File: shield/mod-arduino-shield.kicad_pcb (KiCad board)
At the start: 2 copper layers, 68.7 x 53.3 mm, 49 parts, among them J1 RJHSE-5084, J2 RJHSE-5084, Q1 MMBT3904, U1 SN75176BDR

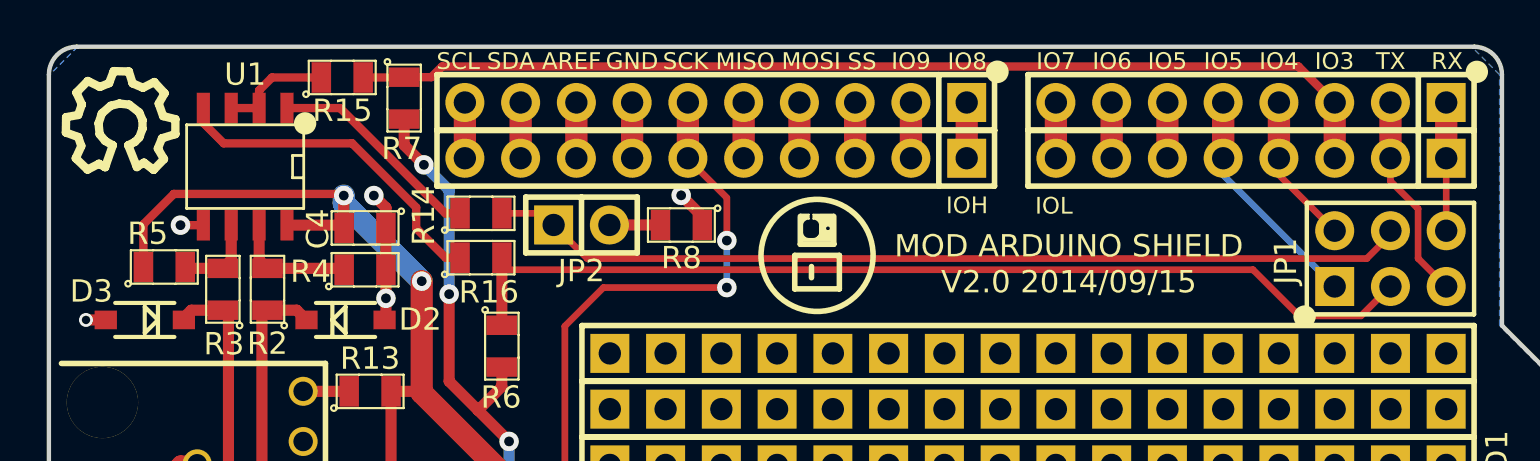
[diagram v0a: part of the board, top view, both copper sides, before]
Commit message: fix issue #3: Add "CC by-SA" license logo to the PCB silk layer Added MOD logo and improved/rearranged previous silk text.
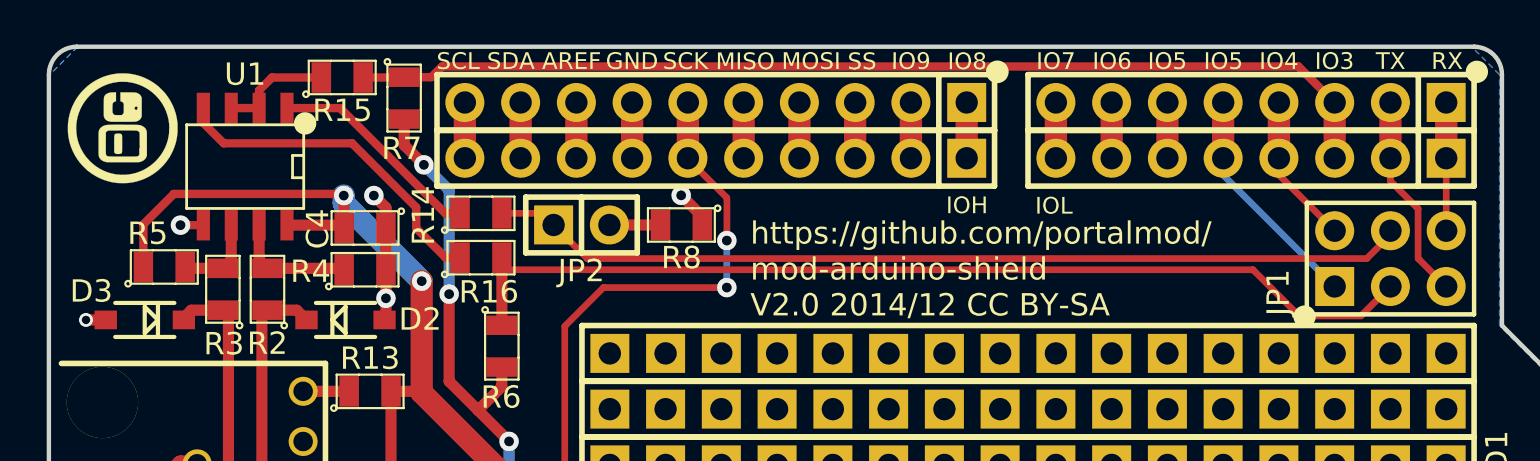
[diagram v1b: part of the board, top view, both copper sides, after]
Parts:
- removed REF***: VAL***, mod-arduino-shield-lib:Symbol_OSHW-Logo_SilkScreen
- added LOGO: LOGO, MOD_Footprints_Lib:MOD_Logo_Small, F.Cu at (99.7, 69.8)
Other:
- board text added: "https://github.com/portalmod/ mod-arduino-shield V2.0 2014/12 CC BY-SA"
- board text removed: "MOD ARDUINO SHIELD V2.0 2014/09/15"

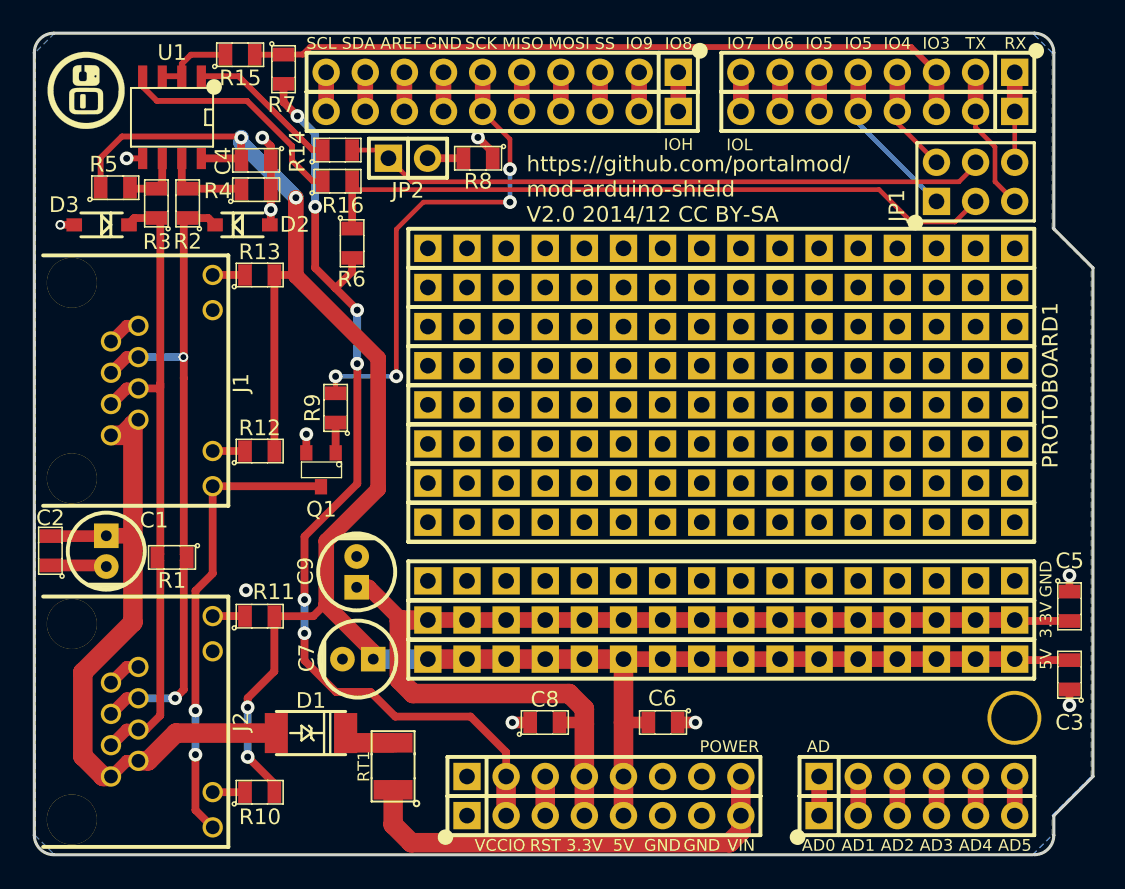
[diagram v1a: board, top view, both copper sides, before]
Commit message: fix issue #6: use same labels on shield as used in arduino
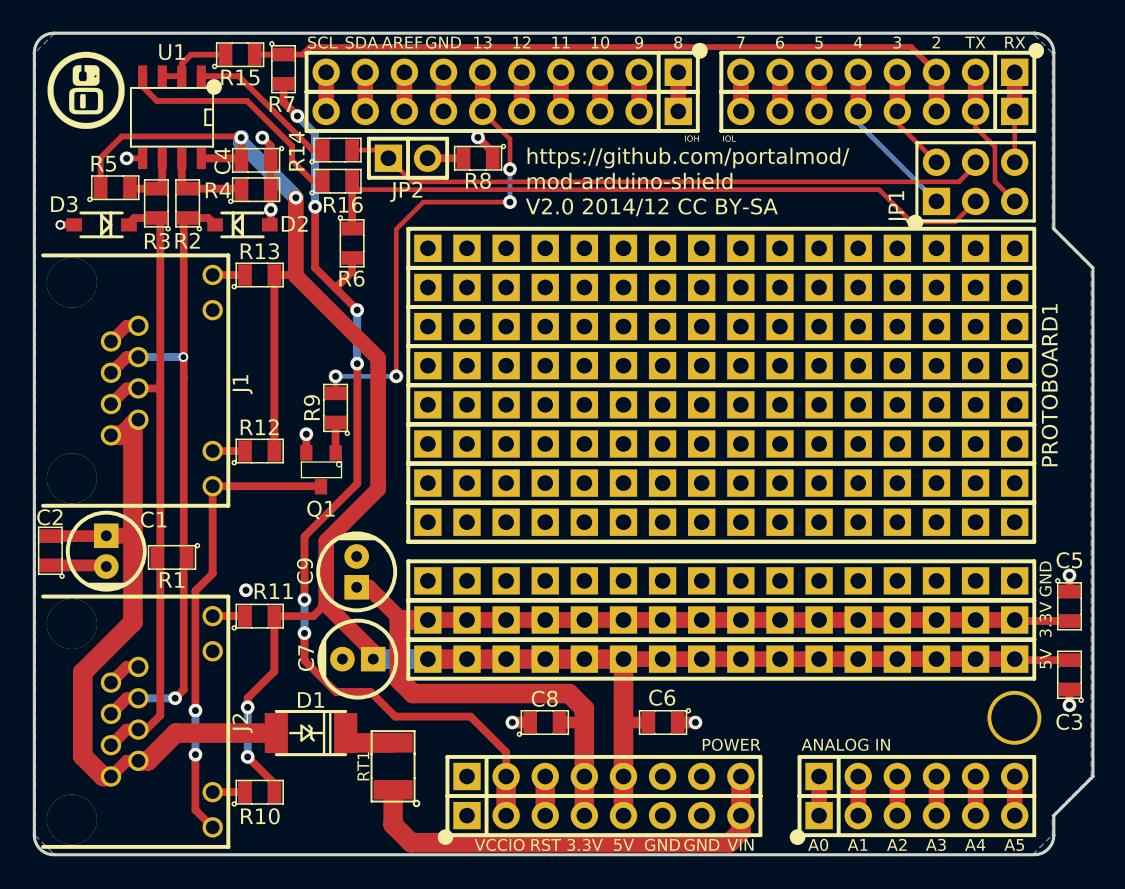
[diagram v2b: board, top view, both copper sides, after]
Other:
- board text added: "10"
- board text added: "11"
- board text added: "12"
- board text added: "13"
- board text added: "2"
- board text added: "3"
- board text added: "4"
- board text added: "5"
- board text added: "6"
- board text added: "7"
- board text added: "8"
- board text added: "9"
- board text added: "A0"
- board text added: "A1"
- board text added: "A2"
- board text added: "A3"
- board text added: "A4"
- board text added: "A5"
- board text added: "ANALOG IN"
- board text removed: "AD"
- board text removed: "AD0"
- board text removed: "AD1"
- board text removed: "AD2"
- board text removed: "AD3"
- board text removed: "AD4"
- board text removed: "AD5"
- board text removed: "IO3"
- board text removed: "IO4"
- board text removed: "IO5"
- board text removed: "IO6"
- board text removed: "IO7"
- board text removed: "IO8"
- board text removed: "IO9"
- board text removed: "MISO"
- board text removed: "MOSI"
- board text removed: "SCK"
- board text removed: "SS"

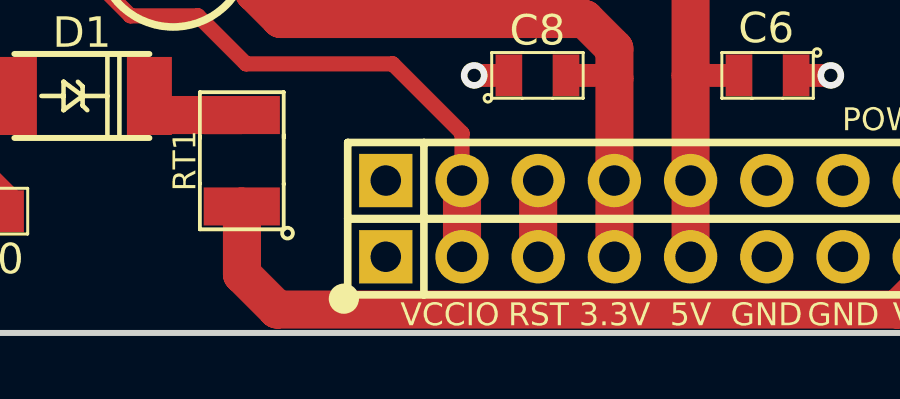
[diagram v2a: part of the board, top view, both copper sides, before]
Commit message: fix issue #2: rename VCCIO to IOREF
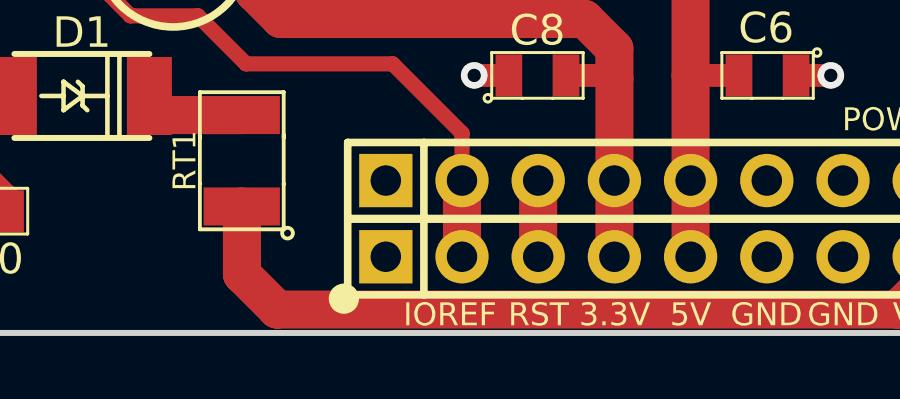
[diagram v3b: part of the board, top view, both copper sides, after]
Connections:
- net VCCIO renamed IOREF
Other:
- board text added: "IOREF"
- board text removed: "VCCIO"

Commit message: fix issue #1: IOREF should not be used to power the circuit
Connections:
- net VIN renamed 9V
- R6 pad 2: IOREF -> 5V
- R7 pad 2: IOREF -> 5V
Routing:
- net IOREF: track 63.1 -> 2.72 mm, vias 6 -> 0
- net 5V: track 142.6 -> 152.6 mm, vias 5 -> 6
